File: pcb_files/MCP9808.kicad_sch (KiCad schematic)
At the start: 2 parts, among them U18 MCP9808T-E_MC

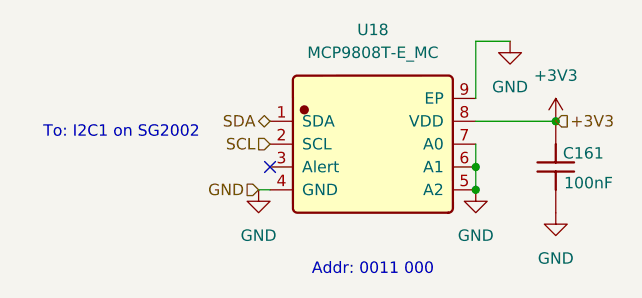
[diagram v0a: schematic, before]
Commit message: Basic Function Review/Documentation for MCP9808
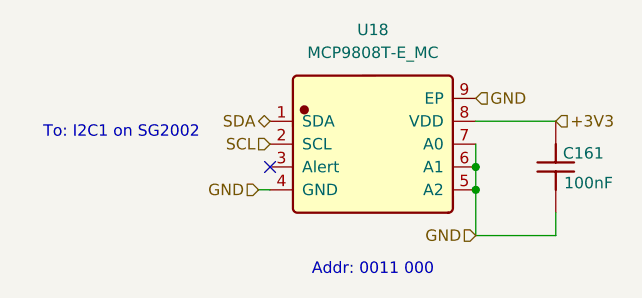
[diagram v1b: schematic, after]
